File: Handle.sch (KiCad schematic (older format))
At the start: 1 part

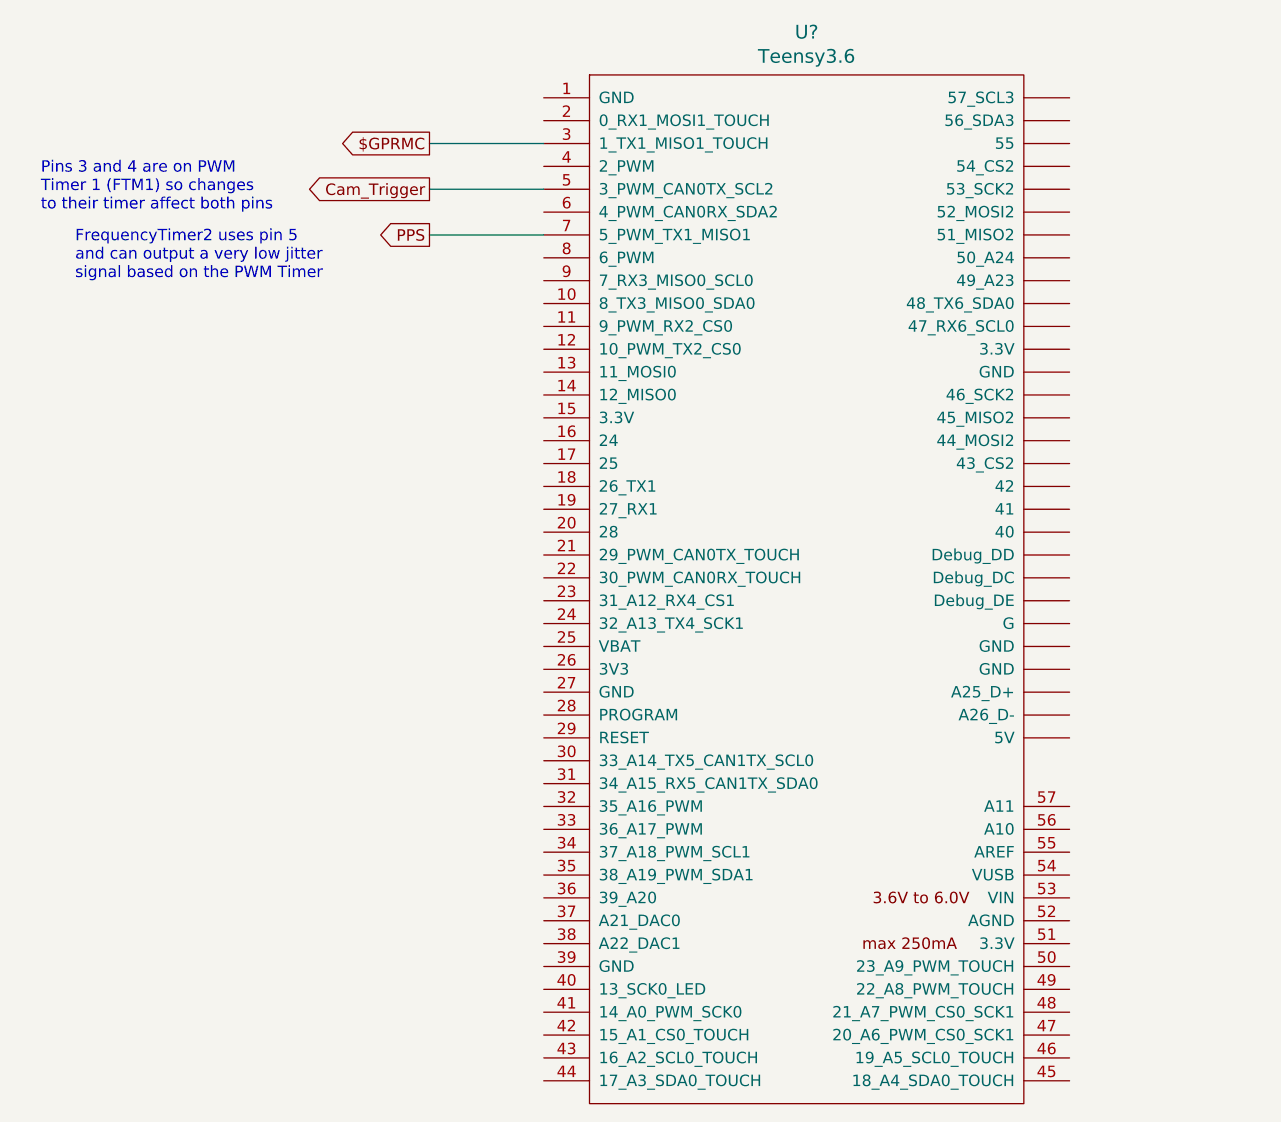
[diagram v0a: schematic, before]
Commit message: Documented pins for tirggering
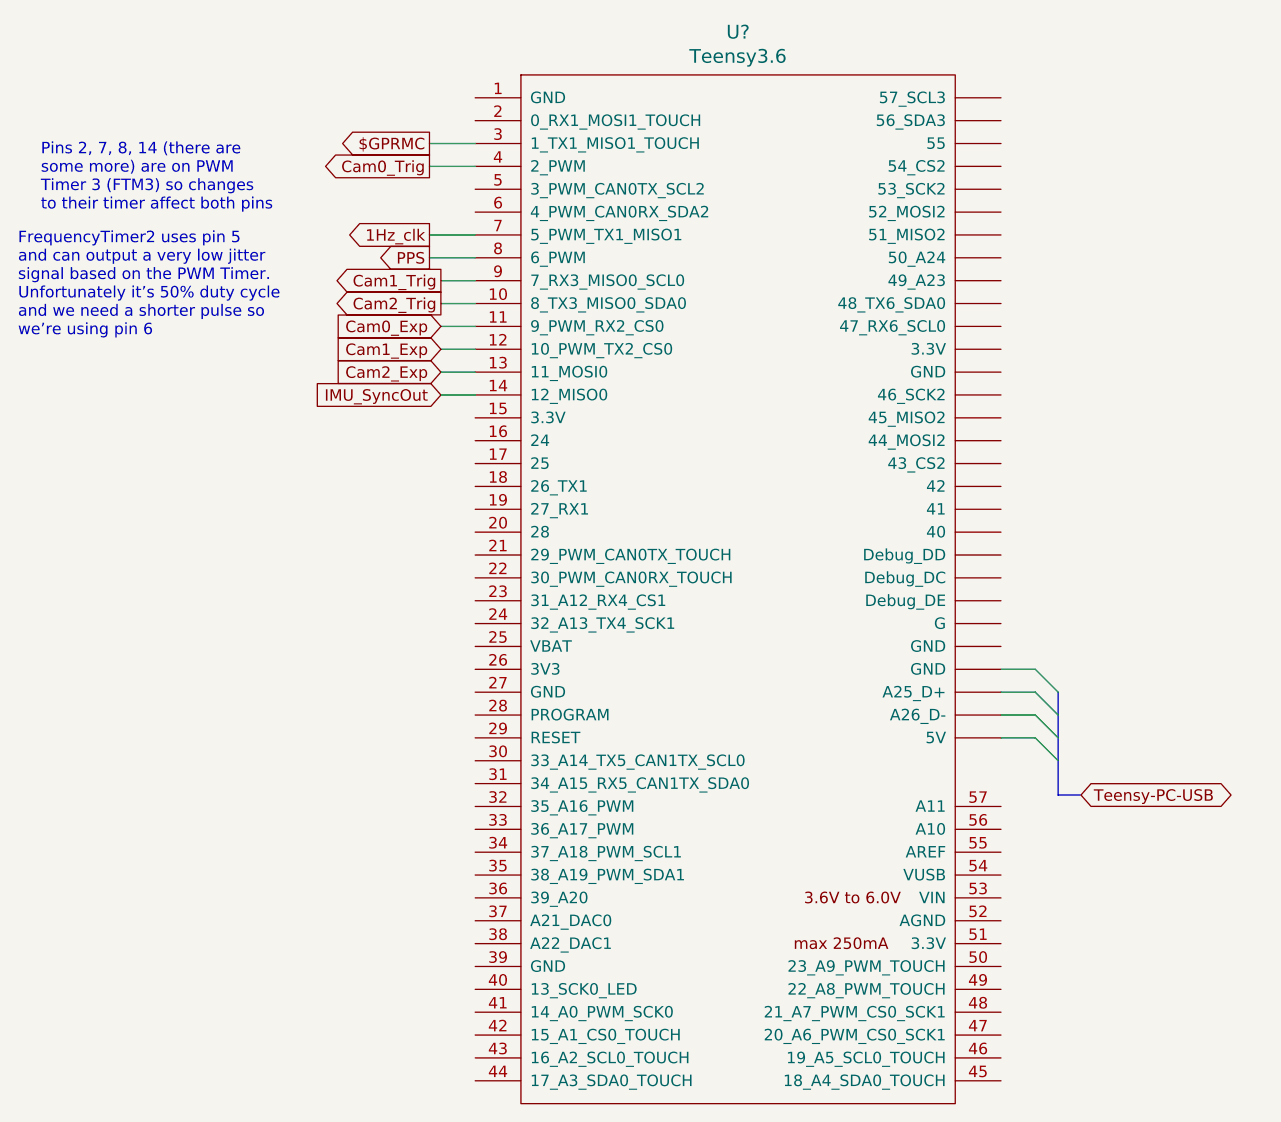
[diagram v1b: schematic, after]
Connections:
- net PPS: now also U?.8 (6_PWM); no longer U?.7 (5_PWM_TX1_MISO1)
- net Cam2_Trig: now reaches U?.10 (8_TX3_MISO0_SDA0)
- net Cam0_Exp: now reaches U?.11 (9_PWM_RX2_CS0)
- net Cam1_Exp: now reaches U?.12 (10_PWM_TX2_CS0)
- net Cam2_Exp: now reaches U?.13 (11_MOSI0)
- net IMU_SyncOut: now reaches U?.14 (12_MISO0)
- net Cam0_Trig: now reaches U?.4 (2_PWM)
- net Cam1_Trig: now reaches U?.9 (7_RX3_MISO0_SCL0)
- net Cam_Trigger: no longer names the net of U?.5 (3_PWM_CAN0TX_SCL2)
- new net 1Hz_clk: U?.7 (5_PWM_TX1_MISO1)
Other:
- note added: "FrequencyTimer2 uses pin 5\nand can output a very low jitter \nsignal based on the PWM Timer.\nUnfortunately it’s 50% duty cycle\nand we need a shorter pulse so \nwe’re using pin 6"
- note added: "Pins 2, 7, 8, 14 (there are\nsome more) are on PWM\nTimer 3 (FTM3) so changes\nto their timer affect both pins"
- note removed: "FrequencyTimer2 uses pin 5\nand can output a very low jitter \nsignal based on the PWM Timer"
- note removed: "Pins 3 and 4 are on PWM\nTimer 1 (FTM1) so changes\nto their timer affect both pins"
- moved on the sheet: U?

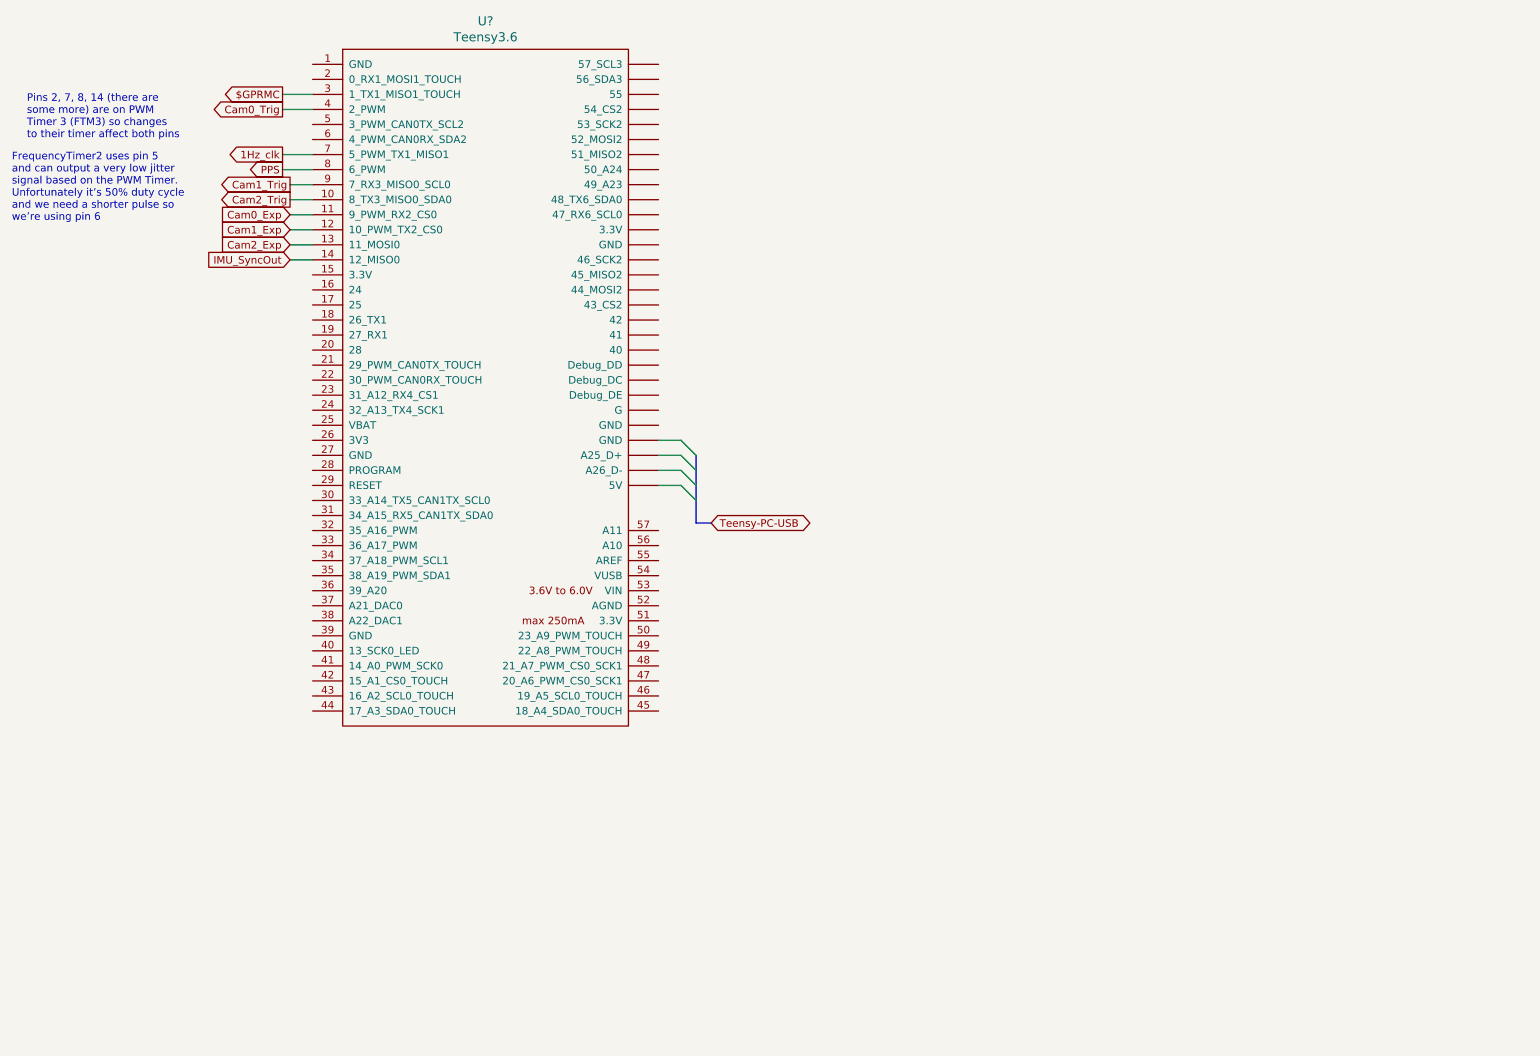
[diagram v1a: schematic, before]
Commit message: Added pinouts for a 4th camera
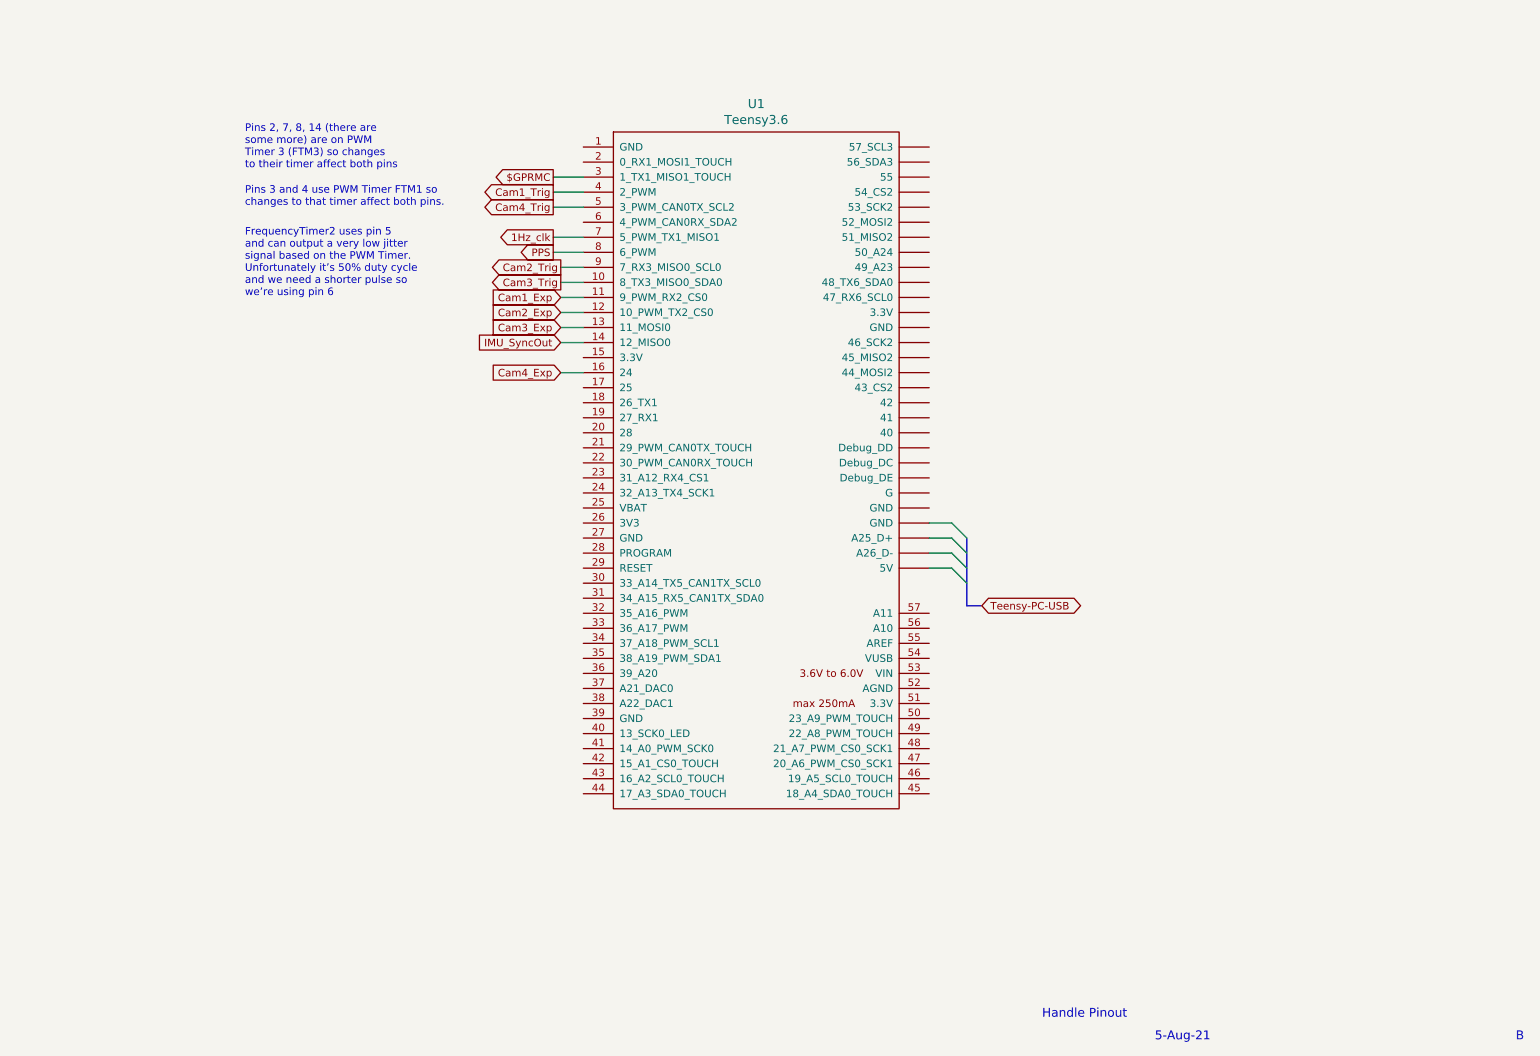
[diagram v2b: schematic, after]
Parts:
- gave numbers to parts that had none: 1
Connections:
- net Cam0_Exp is gone; now on net Cam1_Exp: U1.11 (9_PWM_RX2_CS0)
- net Cam0_Trig is gone; now on net Cam1_Trig: U1.4 (2_PWM)
- net Cam1_Exp: no longer U1.12 (10_PWM_TX2_CS0)
- net Cam1_Trig: no longer U1.9 (7_RX3_MISO0_SCL0)
- net Cam2_Exp: now also U1.12 (10_PWM_TX2_CS0); no longer U1.13 (11_MOSI0)
- net Cam2_Trig: now also U1.9 (7_RX3_MISO0_SCL0); no longer U1.10 (8_TX3_MISO0_SDA0)
- net Cam4_Exp: now reaches U1.16 (24)
- net Cam4_Trig: now reaches U1.5 (3_PWM_CAN0TX_SCL2)
- new net Cam3_Exp: U1.13 (11_MOSI0)
- new net Cam3_Trig: U1.10 (8_TX3_MISO0_SDA0)
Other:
- note added: "5-Aug-21"
- note added: "B"
- note added: "Handle Pinout"
- note added: "Pins 3 and 4 use PWM Timer FTM1 so\nchanges to that timer affect both pins."
- moved on the sheet: U1
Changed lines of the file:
@@
 Comment4 ""
 $EndDescr
-$Comp
-L teensy:Teensy3.6 U?
-U 1 1 5FFCE603
-P 3700 3300
-F 0 "U?" H 3700 5737 60  0000 C CNN
-F 1 "Teensy3.6" H 3700 5631 60  0000 C CNN
-F 2 "" H 3700 3350 60  0000 C CNN
-F 3 "" H 3700 3350 60  0000 C CNN
-	1    3700 3300
-	1    0    0    -1
-$EndComp
 Wire Wire Line
-	2550 1850 2350 1850
-Text GLabel 2350 1850 0    50   Output ~ 0
+	4350 2400 4150 2400
+Text GLabel 4150 2400 0    50   Output ~ 0
 PPS
-Text Notes 550  2200 0    50   ~ 0
+Text Notes 2100 2700 0    50   ~ 0
 FrequencyTimer2 uses pin 5\nand can output a very low jitter \nsignal based on the PWM Timer.\nUnfortunately it’s 50% duty cycle\nand we need a shorter pulse so \nwe’re using pin 6
-Text GLabel 2350 1350 0    50   Output ~ 0
+Text GLabel 4150 1900 0    50   Output ~ 0
 $GPRMC
 Wire Wire Line
-	2350 1350 2550 1350
-Text Notes 650  1650 0    50   ~ 0
+	4150 1900 4350 1900
+Text Notes 2100 1850 0    50   ~ 0
 Pins 2, 7, 8, 14 (there are\nsome more) are on PWM\nTimer 3 (FTM3) so changes\nto their timer affect both pins
+Wire Wire Line
+	4150 2000 4350 2000
+Text GLabel 4150 2000 0    50   Output ~ 0
+Cam1_Trig
+Text GLabel 4150 2300 0    50   Output ~ 0
+1Hz_clk
+Wire Wire Line
+	4150 2300 4350 2300
+Text GLabel 4200 2500 0    50   Output ~ 0
+Cam2_Trig
+Text GLabel 4200 2600 0    50   Output ~ 0
+Cam3_Trig
+Wire Wire Line
+	4200 2500 4350 2500
+Wire Wire Line
+	4350 2600 4200 2600
+Text GLabel 4200 2700 0    50   Input ~ 0
+Cam1_Exp
+Wire Wire Line
+	4200 2700 4350 2700
+Text GLabel 4200 2800 0    50   Input ~ 0
+Cam2_Exp
+Text GLabel 4200 2900 0    50   Input ~ 0
+Cam3_Exp
+Wire Wire Line
+	4200 2900 4350 2900
+Wire Wire Line
+	4200 2800 4350 2800
+Text GLabel 4200 3000 0    50   Input ~ 0
+IMU_SyncOut
+Wire Wire Line
+	4350 3000 4200 3000
+Wire Wire Line
+	6650 4400 6800 4400
+Wire Wire Line
+	6800 4300 6650 4300
+Entry Wire Line
+	6800 4400 6900 4500
+Entry Wire Line
+	6800 4300 6900 4400
+Entry Wire Line
+	6800 4200 6900 4300
+Entry Wire Line
+	6800 4500 6900 4600
+Wire Wire Line
+	6800 4500 6650 4500
+Wire Wire Line
+	6800 4200 6650 4200
+Text GLabel 7000 4750 2    50   BiDi ~ 0
+Teensy-PC-USB
+Wire Bus Line
+	6900 4750 7000 4750
 $Bitmap
-Pos 9800 1350
+Pos 8550 2350
 Scale 0.600000
 Data
@@
 EndData
 $EndBitmap
-Wire Bus Line
-	5100 4200 5200 4200
-Text GLabel 5200 4200 2    50   BiDi ~ 0
-Teensy-PC-USB
-Wire Wire Line
-	5000 3650 4850 3650
-Wire Wire Line
-	5000 3950 4850 3950
-Entry Wire Line
-	5000 3950 5100 4050
-Entry Wire Line
-	5000 3650 5100 3750
-Entry Wire Line
-	5000 3750 5100 3850
-Entry Wire Line
-	5000 3850 5100 3950
-Wire Wire Line
-	5000 3750 4850 3750
-Wire Wire Line
-	4850 3850 5000 3850
-Wire Wire Line
-	2350 1450 2550 1450
-Text GLabel 2350 1450 0    50   Output ~ 0
-Cam0_Trig
-Text GLabel 2350 1750 0    50   Output ~ 0
-1Hz_clk
-Wire Wire Line
-	2350 1750 2550 1750
-Text GLabel 2400 1950 0    50   Output ~ 0
-Cam1_Trig
-Text GLabel 2400 2050 0    50   Output ~ 0
-Cam2_Trig
-Wire Wire Line
-	2400 1950 2550 1950
-Wire Wire Line
-	2550 2050 2400 2050
-Text GLabel 2400 2150 0    50   Input ~ 0
-Cam0_Exp
-Wire Wire Line
-	2400 2150 2550 2150
-Text GLabel 2400 2250 0    50   Input ~ 0
-Cam1_Exp
-Text GLabel 2400 2350 0    50   Input ~ 0
-Cam2_Exp
-Wire Wire Line
-	2400 2350 2550 2350
+$Comp
+L teensy:Teensy3.6 U1
+U 1 1 5FFCE603
+P 5500 3850
+F 0 "U1" H 5500 6287 60  0000 C CNN
+F 1 "Teensy3.6" H 5500 6181 60  0000 C CNN
+F 2 "" H 5500 3900 60  0000 C CNN
+F 3 "" H 5500 3900 60  0000 C CNN
+	1    5500 3850
+	1    0    0    -1
+$EndComp
+Text GLabel 4150 2100 0    50   Output ~ 0
+Cam4_Trig
 Wire Wire Line
-	2400 2250 2550 2250
-Text GLabel 2400 2450 0    50   Input ~ 0
-IMU_SyncOut
+	4150 2100 4350 2100
+Text GLabel 4200 3200 0    50   Input ~ 0
+Cam4_Exp
 Wire Wire Line
-	2550 2450 2400 2450
+	4200 3200 4350 3200
+Text Notes 2100 2100 0    50   ~ 0
+Pins 3 and 4 use PWM Timer FTM1 so\nchanges to that timer affect both pins.
 Wire Bus Line
-	5100 3750 5100 4200
+	6900 4300 6900 4750
+Text Notes 8150 7650 0    59   ~ 0
+5-Aug-21
+Text Notes 10550 7650 0    59   ~ 0
+B
+Text Notes 7400 7500 0    59   ~ 0
+Handle Pinout
 $EndSCHEMATC
